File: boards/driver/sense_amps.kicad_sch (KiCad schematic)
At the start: 5 parts, among them U1 AD1582BRTZ

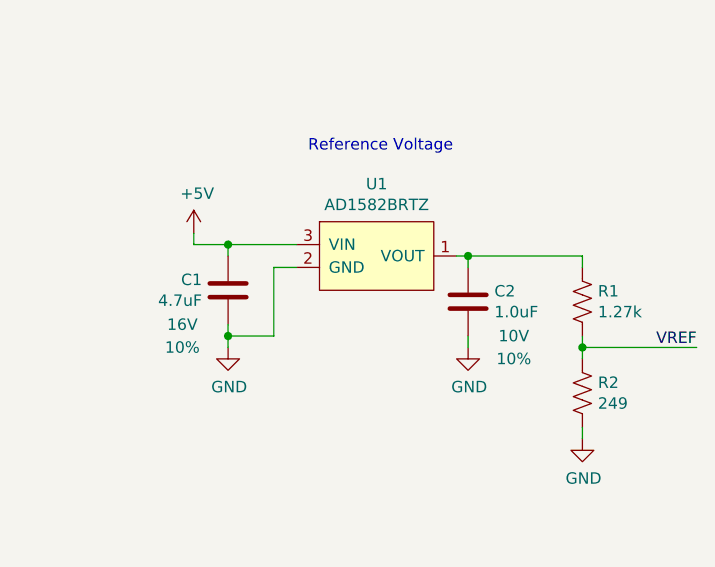
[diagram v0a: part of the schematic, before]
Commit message: Driver: Added a 5V->3.3V LDO to replace the reversed cmod header, added jumpers for the 200R parallel returns, and renamed subcircuit ports to avoid unexpected ground connections.
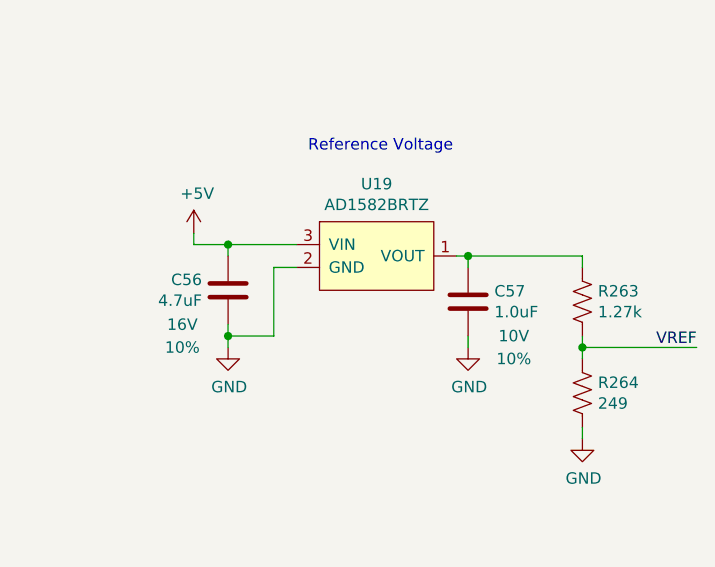
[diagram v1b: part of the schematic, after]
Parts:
- renumbered C1 to C56, C2 to C57, R1 to R263, R2 to R264, U1 to U19
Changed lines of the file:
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@@
   (symbol (lib_id "power:+5V") (at 194.31 83.82 0) (unit 1)
     (in_bom yes) (on_board yes)
-    (property "Reference" "#PWR01" (id 0) (at 194.31 87.63 0)
+    (property "Reference" "#PWR0154" (id 0) (at 194.31 87.63 0)
       (effects (font (size 1.27 1.27)) hide)
     )
@@
   (symbol (lib_id "power:GND") (at 224.79 96.52 0) (unit 1)
     (in_bom yes) (on_board yes)
-    (property "Reference" "#PWR03" (id 0) (at 224.79 102.87 0)
+    (property "Reference" "#PWR0156" (id 0) (at 224.79 102.87 0)
       (effects (font (size 1.27 1.27)) hide)
     )
@@
   (symbol (lib_id "lachesis:AD1582") (at 214.63 87.63 0) (unit 1)
     (in_bom yes) (on_board yes)
-    (property "Reference" "U1" (id 0) (at 214.63 78.359 0))
+    (property "Reference" "U19" (id 0) (at 214.63 78.359 0))
     (property "Value" "AD1582BRTZ" (id 1) (at 214.63 80.6704 0))
     (property "Footprint" "Package_TO_SOT_SMD:SOT-23" (id 2) (at 217.17 87.63 0)
@@
   (symbol (lib_id "Device:C") (at 198.12 90.17 0) (mirror x) (unit 1)
     (in_bom yes) (on_board yes)
-    (property "Reference" "C1" (id 0) (at 195.2244 89.0016 0)
+    (property "Reference" "C56" (id 0) (at 195.2244 89.0016 0)
       (effects (font (size 1.27 1.27)) (justify right))
     )
@@
   (symbol (lib_id "power:GND") (at 198.12 96.52 0) (unit 1)
     (in_bom yes) (on_board yes)
-    (property "Reference" "#PWR02" (id 0) (at 198.12 102.87 0)
+    (property "Reference" "#PWR0155" (id 0) (at 198.12 102.87 0)
       (effects (font (size 1.27 1.27)) hide)
     )
@@
   (symbol (lib_id "Device:C") (at 224.79 91.44 0) (unit 1)
     (in_bom yes) (on_board yes)
-    (property "Reference" "C2" (id 0) (at 227.711 90.2716 0)
+    (property "Reference" "C57" (id 0) (at 227.711 90.2716 0)
       (effects (font (size 1.27 1.27)) (justify left))
     )
@@
   (symbol (lib_id "Device:R_US") (at 237.49 91.44 0) (unit 1)
     (in_bom yes) (on_board yes)
-    (property "Reference" "R1" (id 0) (at 239.2172 90.2716 0)
+    (property "Reference" "R263" (id 0) (at 239.2172 90.2716 0)
       (effects (font (size 1.27 1.27)) (justify left))
     )
@@
   (symbol (lib_id "Device:R_US") (at 237.49 101.6 0) (unit 1)
     (in_bom yes) (on_board yes)
-    (property "Reference" "R2" (id 0) (at 239.2172 100.4316 0)
+    (property "Reference" "R264" (id 0) (at 239.2172 100.4316 0)
       (effects (font (size 1.27 1.27)) (justify left))
     )
@@
   (symbol (lib_id "power:GND") (at 237.49 106.68 0) (unit 1)
     (in_bom yes) (on_board yes)
-    (property "Reference" "#PWR04" (id 0) (at 237.49 113.03 0)
+    (property "Reference" "#PWR0157" (id 0) (at 237.49 113.03 0)
       (effects (font (size 1.27 1.27)) hide)
     )

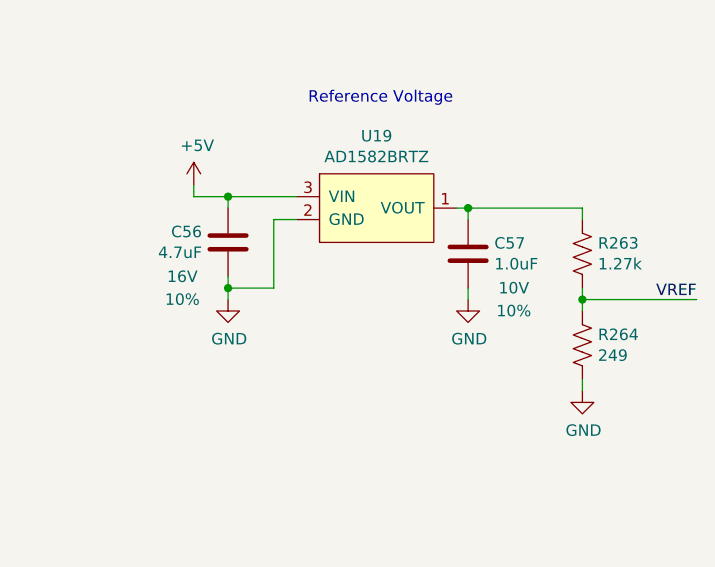
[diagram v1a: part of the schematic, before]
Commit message: Driver: incorporated most changes from the test board, and began layout
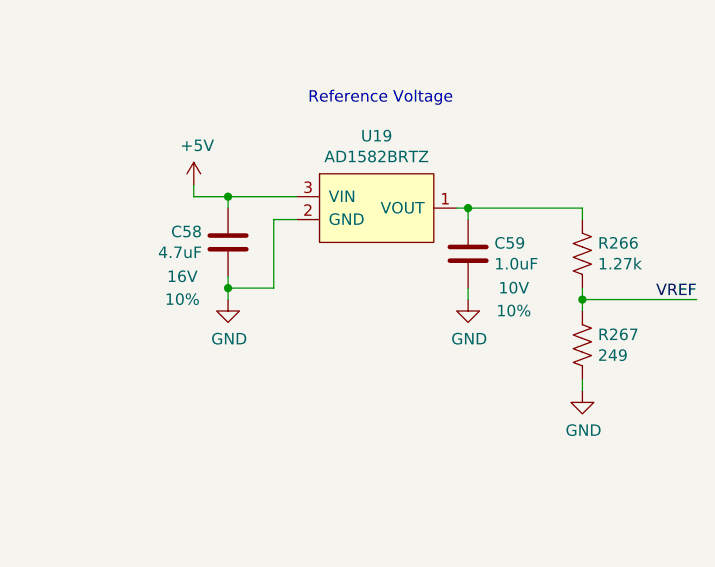
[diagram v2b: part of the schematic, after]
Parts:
- renumbered C56 to C58, C57 to C59, R263 to R266, R264 to R267
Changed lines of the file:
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@@
   (symbol (lib_id "power:+5V") (at 194.31 83.82 0) (unit 1)
     (in_bom yes) (on_board yes)
-    (property "Reference" "#PWR0154" (id 0) (at 194.31 87.63 0)
+    (property "Reference" "#PWR0157" (id 0) (at 194.31 87.63 0)
       (effects (font (size 1.27 1.27)) hide)
     )
@@
   (symbol (lib_id "power:GND") (at 224.79 96.52 0) (unit 1)
     (in_bom yes) (on_board yes)
-    (property "Reference" "#PWR0156" (id 0) (at 224.79 102.87 0)
+    (property "Reference" "#PWR0159" (id 0) (at 224.79 102.87 0)
       (effects (font (size 1.27 1.27)) hide)
     )
@@
   (symbol (lib_id "Device:C") (at 198.12 90.17 0) (mirror x) (unit 1)
     (in_bom yes) (on_board yes)
-    (property "Reference" "C56" (id 0) (at 195.2244 89.0016 0)
+    (property "Reference" "C58" (id 0) (at 195.2244 89.0016 0)
       (effects (font (size 1.27 1.27)) (justify right))
     )
@@
   (symbol (lib_id "power:GND") (at 198.12 96.52 0) (unit 1)
     (in_bom yes) (on_board yes)
-    (property "Reference" "#PWR0155" (id 0) (at 198.12 102.87 0)
+    (property "Reference" "#PWR0158" (id 0) (at 198.12 102.87 0)
       (effects (font (size 1.27 1.27)) hide)
     )
@@
   (symbol (lib_id "Device:C") (at 224.79 91.44 0) (unit 1)
     (in_bom yes) (on_board yes)
-    (property "Reference" "C57" (id 0) (at 227.711 90.2716 0)
+    (property "Reference" "C59" (id 0) (at 227.711 90.2716 0)
       (effects (font (size 1.27 1.27)) (justify left))
     )
@@
   (symbol (lib_id "Device:R_US") (at 237.49 91.44 0) (unit 1)
     (in_bom yes) (on_board yes)
-    (property "Reference" "R263" (id 0) (at 239.2172 90.2716 0)
+    (property "Reference" "R266" (id 0) (at 239.2172 90.2716 0)
       (effects (font (size 1.27 1.27)) (justify left))
     )
@@
   (symbol (lib_id "Device:R_US") (at 237.49 101.6 0) (unit 1)
     (in_bom yes) (on_board yes)
-    (property "Reference" "R264" (id 0) (at 239.2172 100.4316 0)
+    (property "Reference" "R267" (id 0) (at 239.2172 100.4316 0)
       (effects (font (size 1.27 1.27)) (justify left))
     )
@@
   (symbol (lib_id "power:GND") (at 237.49 106.68 0) (unit 1)
     (in_bom yes) (on_board yes)
-    (property "Reference" "#PWR0157" (id 0) (at 237.49 113.03 0)
+    (property "Reference" "#PWR0160" (id 0) (at 237.49 113.03 0)
       (effects (font (size 1.27 1.27)) hide)
     )

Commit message: Driver: laid out most of the subcircuits
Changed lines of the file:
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@@
     (effects (font (size 1.27 1.27)) (justify left bottom))
   )
-  (label "GBR15" (at 123.19 132.08 0)
+  (label "GBR15" (at 57.15 40.64 0)
     (effects (font (size 1.27 1.27)) (justify left bottom))
   )
@@
     (effects (font (size 1.27 1.27)) (justify left bottom))
   )
-  (label "GBR1" (at 57.15 40.64 0)
+  (label "GBR1" (at 57.15 46.99 0)
     (effects (font (size 1.27 1.27)) (justify left bottom))
   )
-  (label "GAR14" (at 123.19 105.41 0)
+  (label "GAR14" (at 123.19 129.54 0)
     (effects (font (size 1.27 1.27)) (justify left bottom))
   )
-  (label "GAR15" (at 123.19 129.54 0)
+  (label "GAR15" (at 57.15 38.1 0)
     (effects (font (size 1.27 1.27)) (justify left bottom))
   )
@@
     (effects (font (size 1.27 1.27)) (justify left bottom))
   )
-  (label "GAR10" (at 123.19 44.45 0)
+  (label "GAR10" (at 123.19 68.58 0)
     (effects (font (size 1.27 1.27)) (justify left bottom))
   )
@@
     (effects (font (size 1.27 1.27)) (justify left bottom))
   )
-  (label "GAR2" (at 57.15 44.45 0)
+  (label "GAR2" (at 57.15 68.58 0)
     (effects (font (size 1.27 1.27)) (justify left bottom))
   )
-  (label "GAR5" (at 57.15 99.06 0)
+  (label "GAR5" (at 57.15 105.41 0)
     (effects (font (size 1.27 1.27)) (justify left bottom))
   )
@@
     (effects (font (size 1.27 1.27)) (justify left bottom))
   )
-  (label "GAR7" (at 57.15 129.54 0)
+  (label "GAR7" (at 57.15 135.89 0)
     (effects (font (size 1.27 1.27)) (justify left bottom))
   )
-  (label "GBR14" (at 123.19 107.95 0)
+  (label "GBR14" (at 123.19 132.08 0)
     (effects (font (size 1.27 1.27)) (justify left bottom))
   )
@@
     (effects (font (size 1.27 1.27)) (justify right bottom))
   )
-  (label "GBR12" (at 123.19 77.47 0)
+  (label "GBR12" (at 123.19 101.6 0)
     (effects (font (size 1.27 1.27)) (justify left bottom))
   )
@@
     (effects (font (size 1.27 1.27)) (justify left bottom))
   )
-  (label "GBR7" (at 57.15 132.08 0)
+  (label "GBR7" (at 57.15 138.43 0)
     (effects (font (size 1.27 1.27)) (justify left bottom))
   )
-  (label "GBR8" (at 57.15 138.43 0)
+  (label "GBR8" (at 123.19 40.64 0)
     (effects (font (size 1.27 1.27)) (justify left bottom))
   )
@@
     (effects (font (size 1.27 1.27)) (justify left bottom))
   )
-  (label "GBR4" (at 57.15 77.47 0)
+  (label "GBR4" (at 57.15 101.6 0)
     (effects (font (size 1.27 1.27)) (justify left bottom))
   )
@@
     (effects (font (size 1.27 1.27)) (justify left bottom))
   )
-  (label "GAR3" (at 57.15 68.58 0)
+  (label "GAR3" (at 57.15 74.93 0)
     (effects (font (size 1.27 1.27)) (justify left bottom))
   )
-  (label "GBR11" (at 123.19 71.12 0)
+  (label "GBR11" (at 123.19 77.47 0)
     (effects (font (size 1.27 1.27)) (justify left bottom))
   )
-  (label "GAR9" (at 123.19 38.1 0)
+  (label "GAR9" (at 123.19 44.45 0)
     (effects (font (size 1.27 1.27)) (justify left bottom))
   )
-  (label "GBR13" (at 123.19 101.6 0)
+  (label "GBR13" (at 123.19 107.95 0)
     (effects (font (size 1.27 1.27)) (justify left bottom))
   )
@@
     (effects (font (size 1.27 1.27)) (justify left bottom))
   )
-  (label "GAR4" (at 57.15 74.93 0)
+  (label "GAR4" (at 57.15 99.06 0)
     (effects (font (size 1.27 1.27)) (justify left bottom))
   )
@@
     (effects (font (size 1.27 1.27)) (justify left bottom))
   )
-  (label "GBR6" (at 57.15 107.95 0)
+  (label "GBR6" (at 57.15 132.08 0)
     (effects (font (size 1.27 1.27)) (justify left bottom))
   )
@@
     (effects (font (size 1.27 1.27)) (justify left bottom))
   )
-  (label "GBR9" (at 123.19 40.64 0)
+  (label "GBR9" (at 123.19 46.99 0)
     (effects (font (size 1.27 1.27)) (justify left bottom))
   )
@@
     (effects (font (size 1.27 1.27)) (justify left bottom))
   )
-  (label "GBR5" (at 57.15 101.6 0)
+  (label "GBR5" (at 57.15 107.95 0)
     (effects (font (size 1.27 1.27)) (justify left bottom))
   )
@@
     (effects (font (size 1.27 1.27)) (justify left bottom))
   )
-  (label "GAR8" (at 57.15 135.89 0)
+  (label "GAR8" (at 123.19 38.1 0)
     (effects (font (size 1.27 1.27)) (justify left bottom))
   )
@@
     (effects (font (size 1.27 1.27)) (justify left bottom))
   )
-  (label "GAR11" (at 123.19 68.58 0)
+  (label "GAR11" (at 123.19 74.93 0)
     (effects (font (size 1.27 1.27)) (justify left bottom))
   )
@@
     (effects (font (size 1.27 1.27)) (justify left bottom))
   )
-  (label "GAR13" (at 123.19 99.06 0)
+  (label "GAR13" (at 123.19 105.41 0)
     (effects (font (size 1.27 1.27)) (justify left bottom))
   )
@@
     (effects (font (size 1.27 1.27)) (justify left bottom))
   )
-  (label "GAR6" (at 57.15 105.41 0)
+  (label "GAR6" (at 57.15 129.54 0)
     (effects (font (size 1.27 1.27)) (justify left bottom))
   )
-  (label "GBR3" (at 57.15 71.12 0)
+  (label "GBR3" (at 57.15 77.47 0)
     (effects (font (size 1.27 1.27)) (justify left bottom))
   )
-  (label "GAR1" (at 57.15 38.1 0)
+  (label "GAR1" (at 57.15 44.45 0)
     (effects (font (size 1.27 1.27)) (justify left bottom))
   )
@@
     (effects (font (size 1.27 1.27)) (justify left bottom))
   )
-  (label "GAR12" (at 123.19 74.93 0)
+  (label "GAR12" (at 123.19 99.06 0)
     (effects (font (size 1.27 1.27)) (justify left bottom))
   )
-  (label "GBR10" (at 123.19 46.99 0)
+  (label "GBR10" (at 123.19 71.12 0)
     (effects (font (size 1.27 1.27)) (justify left bottom))
   )
-  (label "GBR2" (at 57.15 46.99 0)
+  (label "GBR2" (at 57.15 71.12 0)
     (effects (font (size 1.27 1.27)) (justify left bottom))
   )

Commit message: Driver: lightly reorganized FPGA wiring to make it easier to change in the future, and fixed sense amp mapping
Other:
- note added: "40620"
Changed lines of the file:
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@@
+    (effects (font (size 1.27 1.27)) (justify left bottom))
+  )
+  (text "40620" (at 199.39 77.47 0)
     (effects (font (size 1.27 1.27)) (justify left bottom))
   )
@@
     (effects (font (size 1.27 1.27)) (justify left bottom))
   )
-  (label "SA10" (at 156.21 45.72 0)
+  (label "SA10" (at 156.21 69.85 0)
     (effects (font (size 1.27 1.27)) (justify left bottom))
   )
-  (label "SA14" (at 156.21 106.68 0)
+  (label "SA14" (at 156.21 130.81 0)
     (effects (font (size 1.27 1.27)) (justify left bottom))
   )
@@
     (effects (font (size 1.27 1.27)) (justify right bottom))
   )
-  (label "SA7" (at 90.17 130.81 0)
+  (label "SA7" (at 90.17 137.16 0)
     (effects (font (size 1.27 1.27)) (justify left bottom))
   )
@@
     (effects (font (size 1.27 1.27)) (justify left bottom))
   )
-  (label "SA5" (at 90.17 100.33 0)
+  (label "SA5" (at 90.17 106.68 0)
     (effects (font (size 1.27 1.27)) (justify left bottom))
   )
-  (label "SA6" (at 90.17 106.68 0)
+  (label "SA6" (at 90.17 130.81 0)
     (effects (font (size 1.27 1.27)) (justify left bottom))
   )
@@
     (effects (font (size 1.27 1.27)) (justify left bottom))
   )
-  (label "SA13" (at 156.21 100.33 0)
+  (label "SA13" (at 156.21 106.68 0)
     (effects (font (size 1.27 1.27)) (justify left bottom))
   )
@@
     (effects (font (size 1.27 1.27)) (justify left bottom))
   )
-  (label "SA3" (at 90.17 69.85 0)
+  (label "SA3" (at 90.17 76.2 0)
     (effects (font (size 1.27 1.27)) (justify left bottom))
   )
-  (label "SA15" (at 156.21 130.81 0)
+  (label "SA15" (at 90.17 39.37 0)
     (effects (font (size 1.27 1.27)) (justify left bottom))
   )
@@
     (effects (font (size 1.27 1.27)) (justify left bottom))
   )
-  (label "SA9" (at 156.21 39.37 0)
+  (label "SA9" (at 156.21 45.72 0)
     (effects (font (size 1.27 1.27)) (justify left bottom))
   )
@@
     (effects (font (size 1.27 1.27)) (justify left bottom))
   )
-  (label "SA2" (at 90.17 45.72 0)
+  (label "SA2" (at 90.17 69.85 0)
     (effects (font (size 1.27 1.27)) (justify left bottom))
   )
@@
     (effects (font (size 1.27 1.27)) (justify left bottom))
   )
-  (label "SA12" (at 156.21 76.2 0)
+  (label "SA12" (at 156.21 100.33 0)
     (effects (font (size 1.27 1.27)) (justify left bottom))
   )
@@
     (effects (font (size 1.27 1.27)) (justify left bottom))
   )
-  (label "SA11" (at 156.21 69.85 0)
+  (label "SA11" (at 156.21 76.2 0)
     (effects (font (size 1.27 1.27)) (justify left bottom))
   )
@@
     (effects (font (size 1.27 1.27)) (justify left bottom))
   )
-  (label "SA4" (at 90.17 76.2 0)
+  (label "SA4" (at 90.17 100.33 0)
     (effects (font (size 1.27 1.27)) (justify left bottom))
   )
@@
     (effects (font (size 1.27 1.27)) (justify left bottom))
   )
-  (label "SA8" (at 90.17 137.16 0)
+  (label "SA8" (at 156.21 39.37 0)
     (effects (font (size 1.27 1.27)) (justify left bottom))
   )
@@
     (effects (font (size 1.27 1.27)) (justify left bottom))
   )
-  (label "SA1" (at 90.17 39.37 0)
+  (label "SA1" (at 90.17 45.72 0)
     (effects (font (size 1.27 1.27)) (justify left bottom))
   )

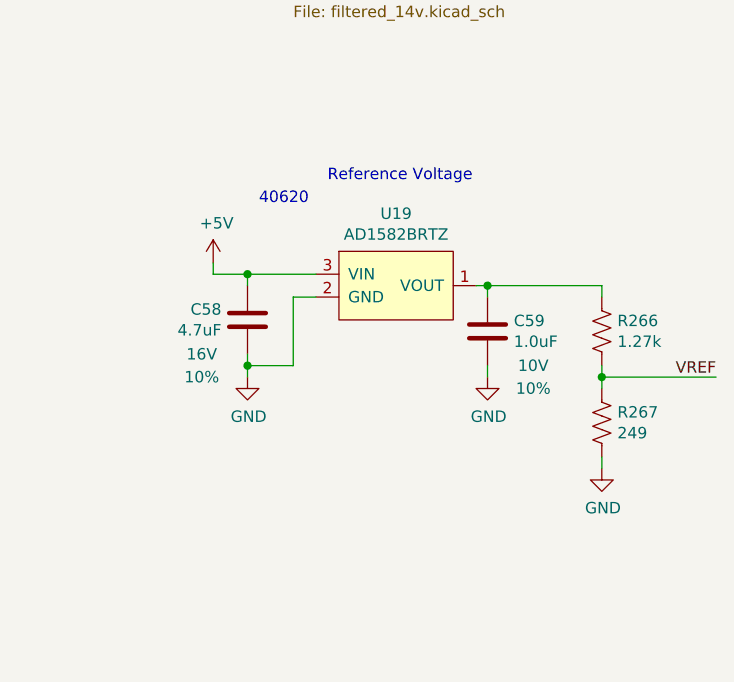
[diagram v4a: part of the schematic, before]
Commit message: Driver: incorporated completed backplane pinout and did a little bit more routing on the board
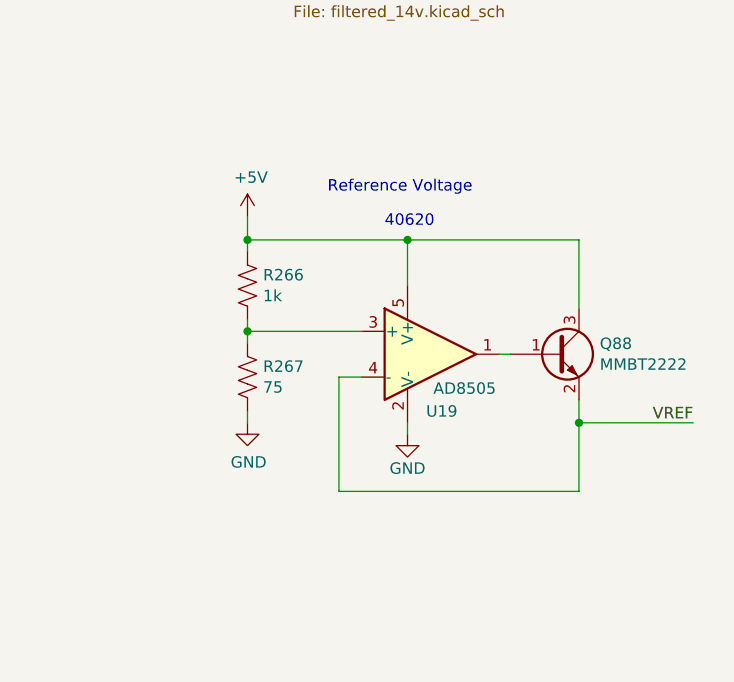
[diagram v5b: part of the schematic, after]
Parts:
- removed C58: 4.7uF, Capacitor_SMD:C_0805_2012Metric, symbol Device:C
- removed C59: 1.0uF, Capacitor_SMD:C_0603_1608Metric, symbol Device:C
- removed U19: AD1582BRTZ, Package_TO_SOT_SMD:SOT-23, symbol lachesis:AD1582
- added Q88: MMBT2222, Package_TO_SOT_SMD:SOT-23, symbol Device:Q_NPN_BEC
- added U19: AD8505, Package_TO_SOT_SMD:SOT-23-5, symbol lachesis:AD8505
- R266: value 1.27k -> 1k
- R267: value 249 -> 75
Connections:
- net +5V: now also R266.1, Q88.3 (C), U19.5 (V+)
- net GND: now also U19.2 (V-)
- net VREF: now also Q88.2 (E), U19.4 (-); no longer R266.2, R267.1
- new net: R266.2, R267.1, U19.3 (+)
- new net: Q88.1 (B), U19.1
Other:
- moved on the sheet: R266, R267

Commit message: Driver: minor schematic cleanup and populated all of the BOM except for resistors
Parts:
- Q88: MPN (none) -> MMBT2222ALT1HTSA1; Manufacturer (none) -> Infineon Technologies; Package (none) -> SOT-23-3
- U19: MPN (none) -> AD8505ARJZ-R7; Manufacturer (none) -> Analog Devices, Inc; Package (none) -> SOT-23-5
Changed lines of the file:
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@@
   (symbol (lib_id "power:+5V") (at 198.12 78.74 0) (unit 1)
     (in_bom yes) (on_board yes)
-    (property "Reference" "#PWR0157" (id 0) (at 198.12 82.55 0)
+    (property "Reference" "#PWR0159" (id 0) (at 198.12 82.55 0)
       (effects (font (size 1.27 1.27)) hide)
     )
@@
   (symbol (lib_id "power:GND") (at 198.12 101.6 0) (unit 1)
     (in_bom yes) (on_board yes)
-    (property "Reference" "#PWR0158" (id 0) (at 198.12 107.95 0)
+    (property "Reference" "#PWR0160" (id 0) (at 198.12 107.95 0)
       (effects (font (size 1.27 1.27)) hide)
     )
@@
       (effects (font (size 1.27 1.27)) hide)
     )
+    (property "MPN" "MMBT2222ALT1HTSA1" (id 6) (at 232.41 93.98 0)
+      (effects (font (size 1.27 1.27)) hide)
+    )
+    (property "Manufacturer" "Infineon Technologies" (id 7) (at 232.41 93.98 0)
+      (effects (font (size 1.27 1.27)) hide)
+    )
+    (property "Description" "TRANS NPN 40V 0.6A SOT-23" (id 8) (at 232.41 93.98 0)
+      (effects (font (size 1.27 1.27)) hide)
+    )
+    (property "Package" "SOT-23-3" (id 9) (at 232.41 93.98 0)
+      (effects (font (size 1.27 1.27)) hide)
+    )
     (pin "1")
     (pin "2")
@@
   (symbol (lib_id "power:GND") (at 215.9 102.87 0) (unit 1)
     (in_bom yes) (on_board yes)
-    (property "Reference" "#PWR0159" (id 0) (at 215.9 109.22 0)
+    (property "Reference" "#PWR0161" (id 0) (at 215.9 109.22 0)
       (effects (font (size 1.27 1.27)) hide)
     )
@@
       (effects (font (size 1.27 1.27)) hide)
     )
+    (property "MPN" "AD8505ARJZ-R7" (id 4) (at 218.44 93.98 0)
+      (effects (font (size 1.27 1.27)) hide)
+    )
+    (property "Description" "IC OPAMP GP 1 CIRCUIT SOT23-5" (id 5) (at 218.44 93.98 0)
+      (effects (font (size 1.27 1.27)) hide)
+    )
+    (property "Manufacturer" "Analog Devices, Inc" (id 6) (at 218.44 93.98 0)
+      (effects (font (size 1.27 1.27)) hide)
+    )
+    (property "Package" "SOT-23-5" (id 7) (at 218.44 93.98 0)
+      (effects (font (size 1.27 1.27)) hide)
+    )
